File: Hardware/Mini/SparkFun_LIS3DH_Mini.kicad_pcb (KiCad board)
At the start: 2 copper layers, 25.4 x 25.4 mm, 24 parts, among them J1 Conn_01x02, J2 Qwiic_RA, U1 LIS3DH

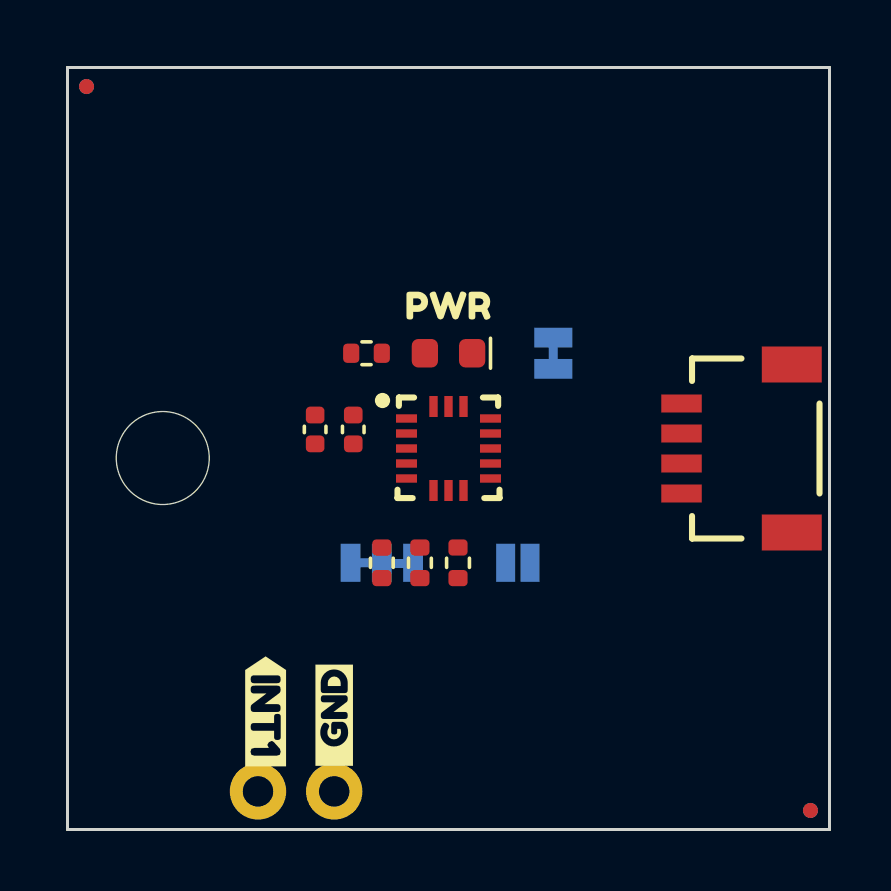
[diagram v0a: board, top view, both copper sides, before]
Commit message: Gets the correct shape of the Micro
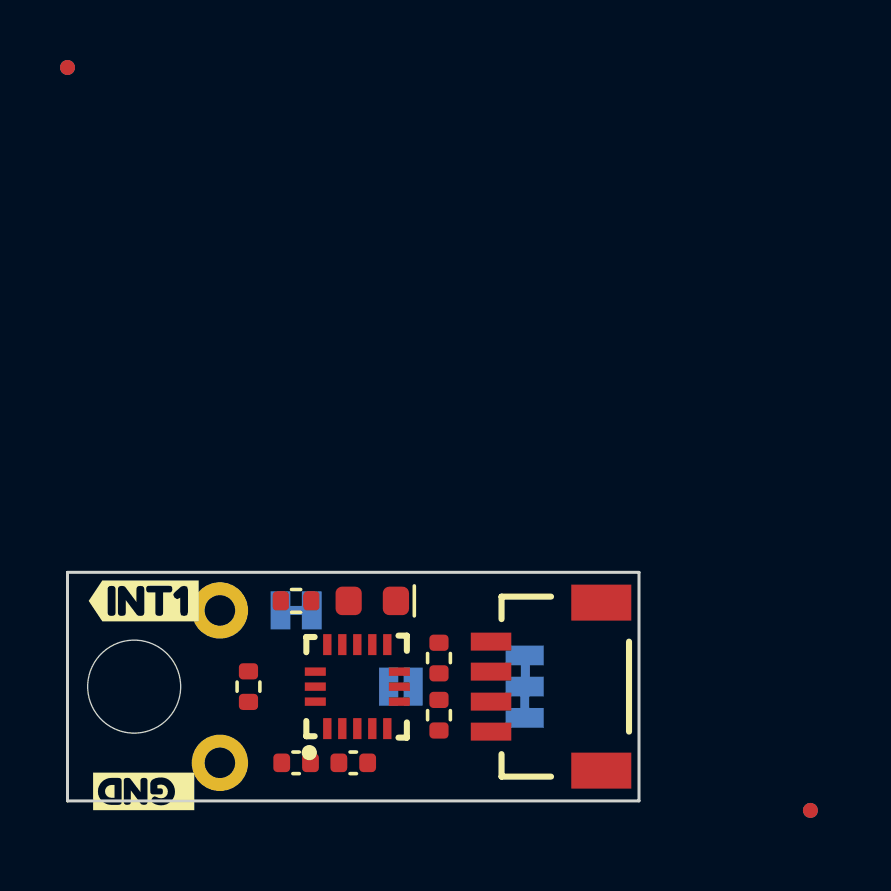
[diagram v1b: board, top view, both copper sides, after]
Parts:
- removed J1: Conn_01x02, SparkFun-Connector:1x02
- removed kibuzzard-65A8A8B4: G***, kibuzzard-65A8A8B4
- added J3: Conn_01x01, SparkFun-Connector:1x01, F.Cu at (128.3, 103.5)
- added J4: Conn_01x01, SparkFun-Connector:1x01, F.Cu at (128.3, 108.6)
- moved JP1 12.1 mm to (130.9, 103.5), turned to 0 degrees
- moved C3 11.1 mm to (130.9, 108.6), turned to 180 degrees
- moved C4 11.1 mm to (132.8, 108.6), turned to 0 degrees
- moved J2 10.2 mm to (137.4, 106.0)
- moved D1 8.64 mm to (133.4, 103.2)
- moved R3 8.58 mm to (130.9, 103.2)
- moved U1 8.50 mm to (132.9, 106.0), turned to 90 degrees
- moved R2 8.11 mm to (129.3, 106.0), turned to 90 degrees
- moved ST1 7.68 mm to (125.5, 106.0)
- moved kibuzzard-6838B97C 6.84 mm to (125.8, 109.5), turned to 180 degrees
- moved kibuzzard-67BF7EBF 6.67 mm to (125.9, 109.5), turned to 180 degrees
- moved JP2 6.30 mm to (138.5, 106.0), turned to 90 degrees
- moved JP3 5.68 mm to (134.4, 106.0)
- moved kibuzzard-6838B753 5.48 mm to (125.8, 103.2), turned to 0 degrees
- moved kibuzzard-6838BA16 5.48 mm to (125.8, 103.2), turned to 180 degrees
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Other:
- board size 25.4 x 25.4 mm -> 19 x 7.6 mm

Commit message: Adds testpoints
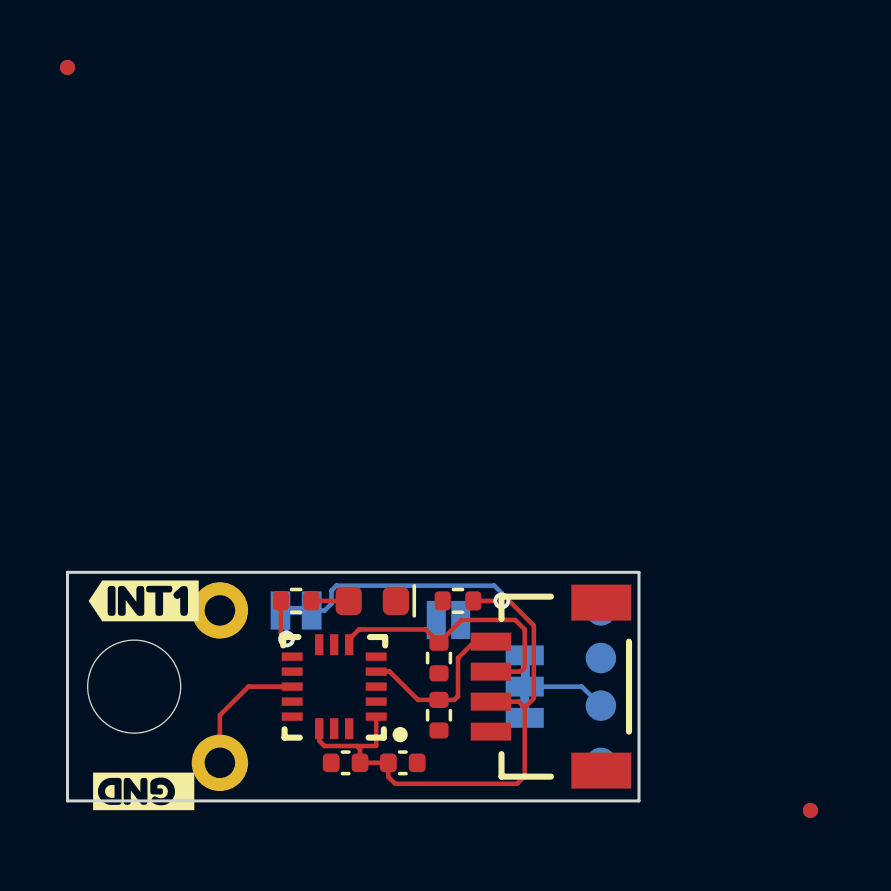
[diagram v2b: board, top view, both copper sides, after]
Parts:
- added TP1: 1.0mm, SparkFun-Connector:TestPoint-1.0mm, B.Cu at (141.0, 103.5)
- added TP2: 1.0mm, SparkFun-Connector:TestPoint-1.0mm, B.Cu at (141.0, 105.1)
- added TP3: 1.0mm, SparkFun-Connector:TestPoint-1.0mm, B.Cu at (141.0, 106.7)
- added TP4: 1.0mm, SparkFun-Connector:TestPoint-1.0mm, B.Cu at (141.0, 108.6)
- moved R2 7.55 mm to (136.3, 103.2), turned to 0 degrees
- moved JP3 2.73 mm to (136.0, 103.8)
- moved C3 1.65 mm to (132.5, 108.6)
- moved C4 1.65 mm to (134.4, 108.6)
- moved U1 0.77 mm to (132.2, 106.0), turned to 180 degrees
- turned R1 to -90 degrees
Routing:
- net 3.3V: track 0.00 -> 28.9 mm, vias 0 -> 1
- net SDA: track 0.00 -> 9.24 mm
- net SCL: track 0.00 -> 5.77 mm
- net INT1: track 0.00 -> 4.39 mm
- net Net-(JP1-A): track 0.00 -> 2.39 mm, vias 0 -> 1
- net Net-(D1-A): track 0.00 -> 1.24 mm

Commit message: Adds 0402 Red LED - reroutes the PCB
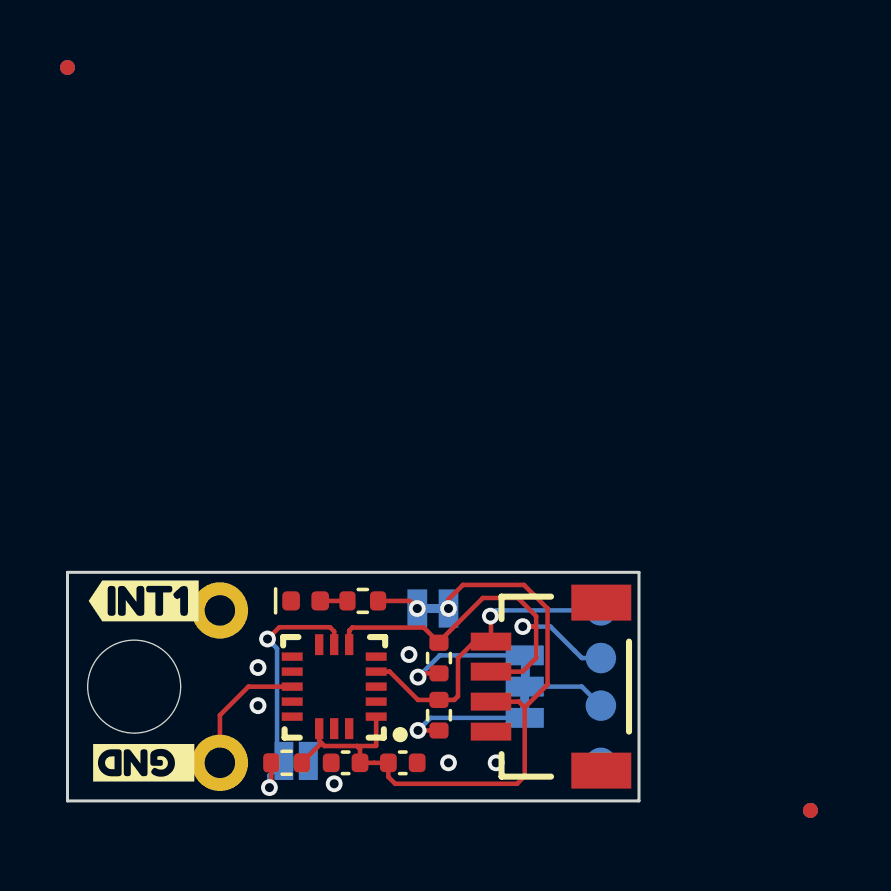
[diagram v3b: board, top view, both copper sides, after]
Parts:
- D1: footprint SparkFun-LED:LED_0603_1608Metric_Red -> SparkFun-LED:LED_0402_1005Metric
- moved R2 7.86 mm to (130.6, 108.6)
- moved JP3 6.92 mm to (130.9, 108.5)
- moved JP1 4.56 mm to (135.4, 103.4)
- moved D1 2.22 mm to (131.2, 103.2), turned to 0 degrees
- moved R3 2.22 mm to (133.1, 103.2), turned to 180 degrees
- moved kibuzzard-67BF7EBF 0.95 mm to (125.9, 108.6)
- moved kibuzzard-6838B97C 0.95 mm to (125.8, 108.6)
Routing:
- net ADDR/SDO: track 0.00 -> 9.11 mm, vias 0 -> 2
- net SDA: track 9.24 -> 14.4 mm, vias 0 -> 1
- net SCL: track 5.77 -> 10.4 mm, vias 0 -> 1
- net Net-(JP2-C): track 0.00 -> 4.61 mm, vias 0 -> 1
- net Net-(JP2-A): track 0.00 -> 4.43 mm, vias 0 -> 1
- net 3.3V: track 28.9 -> 25.1 mm
- net Net-(JP1-A): track 2.39 -> 1.41 mm
- net GND: vias 0 -> 6

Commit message: Positions the testpoints according to their position in every other micro design
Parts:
- removed J3, J4: Conn_01x01, SparkFun-Connector:1x01
- removed TP1, TP2, TP3, TP4: 1.0mm, SparkFun-Connector:TestPoint-1.0mm
- added J1: PTH_1x1mm, SparkFun-Connector:1x01_PTH_1x1mm, F.Cu at (128.3, 109.5)
- added J5: PTH_1x1mm, SparkFun-Connector:1x01_PTH_1x1mm, F.Cu at (128.3, 104.5)
- added TP5: 0.75mm, SparkFun-Connector:TestPoint-0.75mm, B.Cu at (141.3, 104.1)
- added TP6: 0.75mm, SparkFun-Connector:TestPoint-0.75mm, B.Cu at (141.3, 106.0)
- added TP7: 0.75mm, SparkFun-Connector:TestPoint-0.75mm, B.Cu at (141.3, 107.9)
- added TP8: 0.75mm, SparkFun-Connector:TestPoint-0.75mm, B.Cu at (141.3, 109.9)
- moved FID2 18.4 mm to (126.4, 103.6)
- moved FID3 18.4 mm to (126.4, 103.6)
- moved FID1 7.90 mm to (140.3, 108.6)
- moved FID4 7.90 mm to (140.3, 108.6)
- moved C3 0.95 mm to (132.5, 109.5)
- moved C4 0.95 mm to (134.4, 109.5)
- moved J2 0.95 mm to (137.4, 107.0)
- moved JP1 0.95 mm to (135.4, 104.4)
- moved JP2 0.95 mm to (138.5, 107.0)
- moved JP3 0.95 mm to (130.9, 109.5)
- moved R1 0.95 mm to (135.6, 106.0)
- moved R2 0.95 mm to (130.6, 109.5)
- moved R6 0.95 mm to (135.6, 107.9)
- moved ST1 0.95 mm to (125.5, 107.0)
- moved U1 0.95 mm to (132.2, 107.0)
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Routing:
- net SCL: track 10.4 -> 6.90 mm
- net SDA: track 14.4 -> 12.9 mm
- net 3.3V: track 25.1 -> 24.0 mm

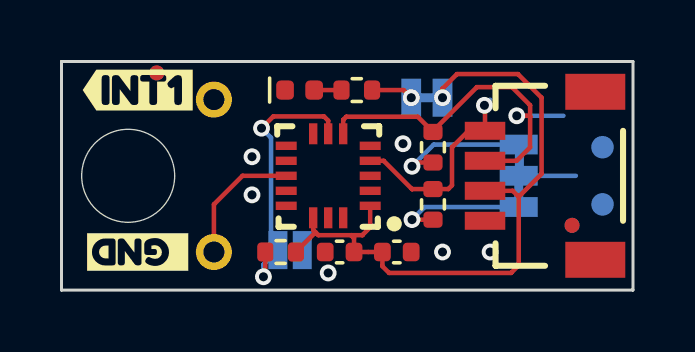
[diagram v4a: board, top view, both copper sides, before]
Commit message: Adds silk
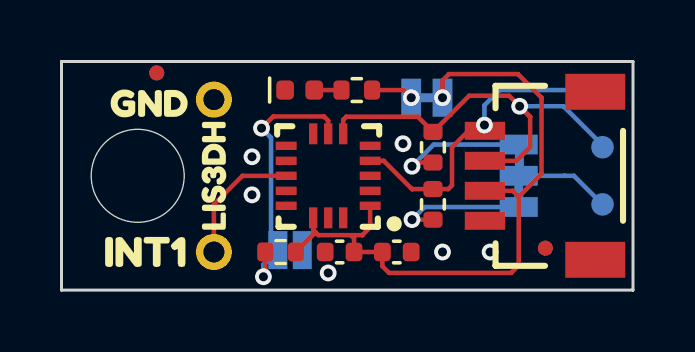
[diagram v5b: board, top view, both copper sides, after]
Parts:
- removed kibuzzard-67BF7EBF: G***, kibuzzard-67BF7EBF
- removed kibuzzard-6838B753: G***, kibuzzard-6838B753
- removed kibuzzard-6838B97C: G***, kibuzzard-6838B97C
- removed kibuzzard-6838BA16: G***, kibuzzard-6838BA16
- added kibuzzard-6841DB16: G***, kibuzzard-6841DB16, F.Cu at (126.1, 109.5)
- added kibuzzard-6841DB2D: G***, kibuzzard-6841DB2D, F.Cu at (126.2, 104.6)
- added kibuzzard-6841DB35: G***, kibuzzard-6841DB35, B.Cu at (126.2, 104.6)
- added kibuzzard-6841DB4C: G***, kibuzzard-6841DB4C, B.Cu at (126.1, 109.5)
- added kibuzzard-6841DC10: G***, kibuzzard-6841DC10, F.Cu at (128.3, 107.0)
- added kibuzzard-6841DC10: G***, kibuzzard-6841DC10, B.Cu at (128.3, 107.0)
- added kibuzzard-6841DC42: G***, kibuzzard-6841DC42, B.Cu at (130.9, 106.6)
- added kibuzzard-6841DC70: G***, kibuzzard-6841DC70, B.Cu at (132.9, 104.5)
- added kibuzzard-6841DC9E: G***, kibuzzard-6841DC9E, B.Cu at (137.0, 107.0)
- moved FID1 1.17 mm to (139.4, 109.4)
- moved FID4 1.17 mm to (139.4, 109.4)
- moved ST1 0.32 mm to (125.8, 107.0)
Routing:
- net SCL: track 6.90 -> 10.8 mm
- net 3.3V: track 24.0 -> 25.5 mm
- net SDA: track 12.9 -> 14.3 mm

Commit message: Adds more silk and adds measure
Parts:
- removed kibuzzard-6841DB35: G***, kibuzzard-6841DB35
- removed kibuzzard-6841DB4C: G***, kibuzzard-6841DB4C
- added G***: LOGO, SparkFun-Aesthetic:qwiic_3mm, B.Cu at (138.6, 103.9)
- added G***: Flame, SparkFun-Aesthetic:SparkFun_Flame_3mm, B.Cu at (133.3, 107.0)
- added Ref**: Val**, SparkFun-Aesthetic:OSHW_Logo_2.5mm, B.Cu at (124.5, 109.8)

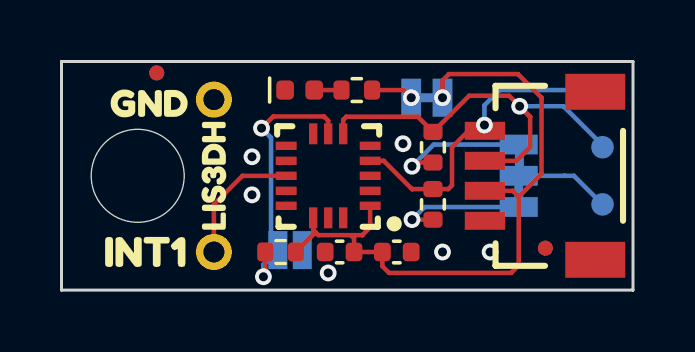
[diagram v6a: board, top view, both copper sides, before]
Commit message: Fixes measures, adjusts some traces
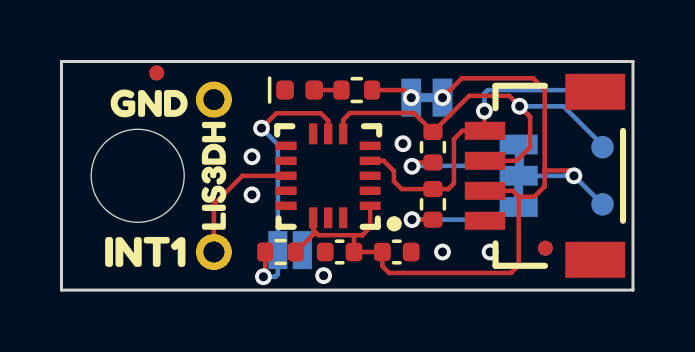
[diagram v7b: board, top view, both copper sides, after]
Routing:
- net 3.3V: track 25.5 -> 26.6 mm, vias 1 -> 2
- net SCL: track 10.8 -> 11.3 mm
